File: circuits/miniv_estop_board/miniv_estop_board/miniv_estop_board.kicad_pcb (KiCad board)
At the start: 2 copper layers, 100 x 130 mm, 39 parts, among them J1 Conn_Main_DCDC, J2 Conn_neopixel_01, J3 Conn_neopixel_02, J4 Conn_neopixel_03, J5 Conn_neopixel_04, J6 EStop_button, J7 EStop_signal0, J8 EStop_signal1, Q1 2SJ555-E, Q2 NPN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

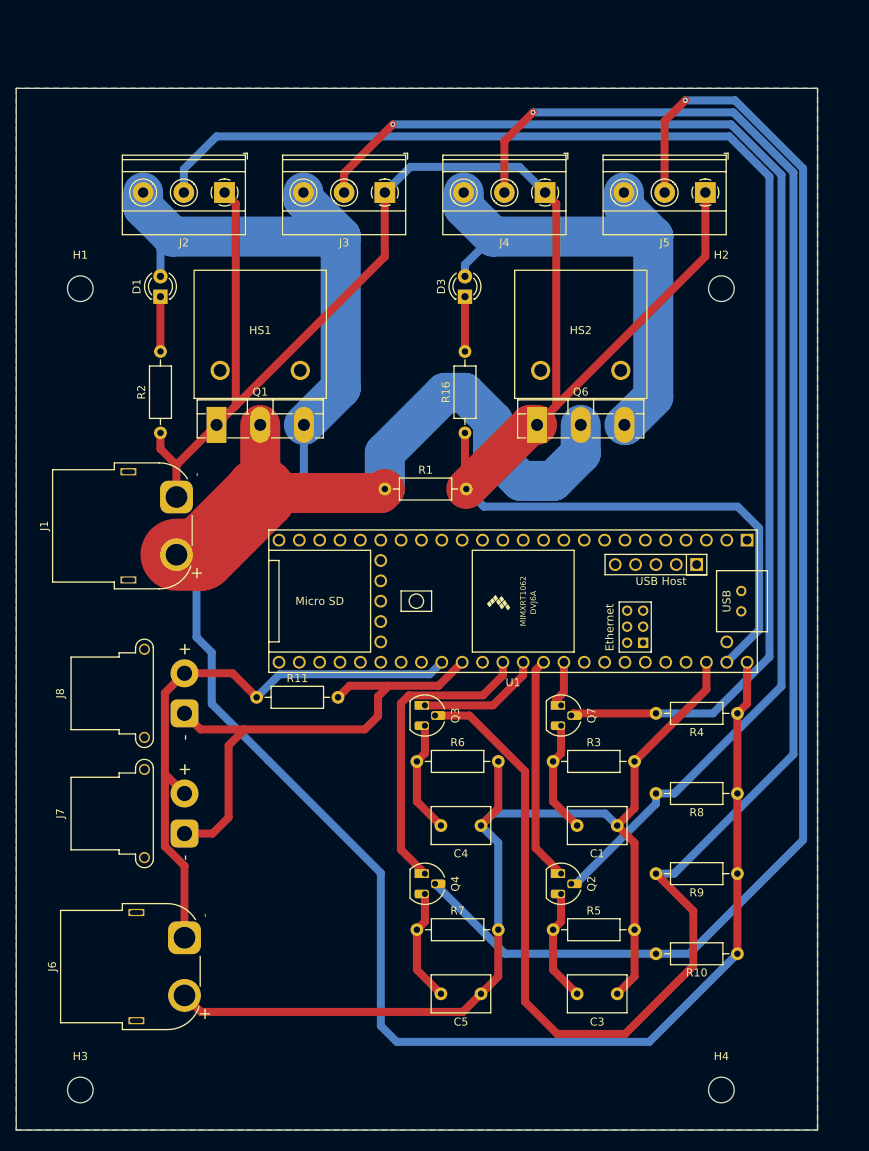
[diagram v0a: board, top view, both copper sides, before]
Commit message: modify connection
Signed-off-by: Masaya Kataoka <ms.kataoka@gmail.com>
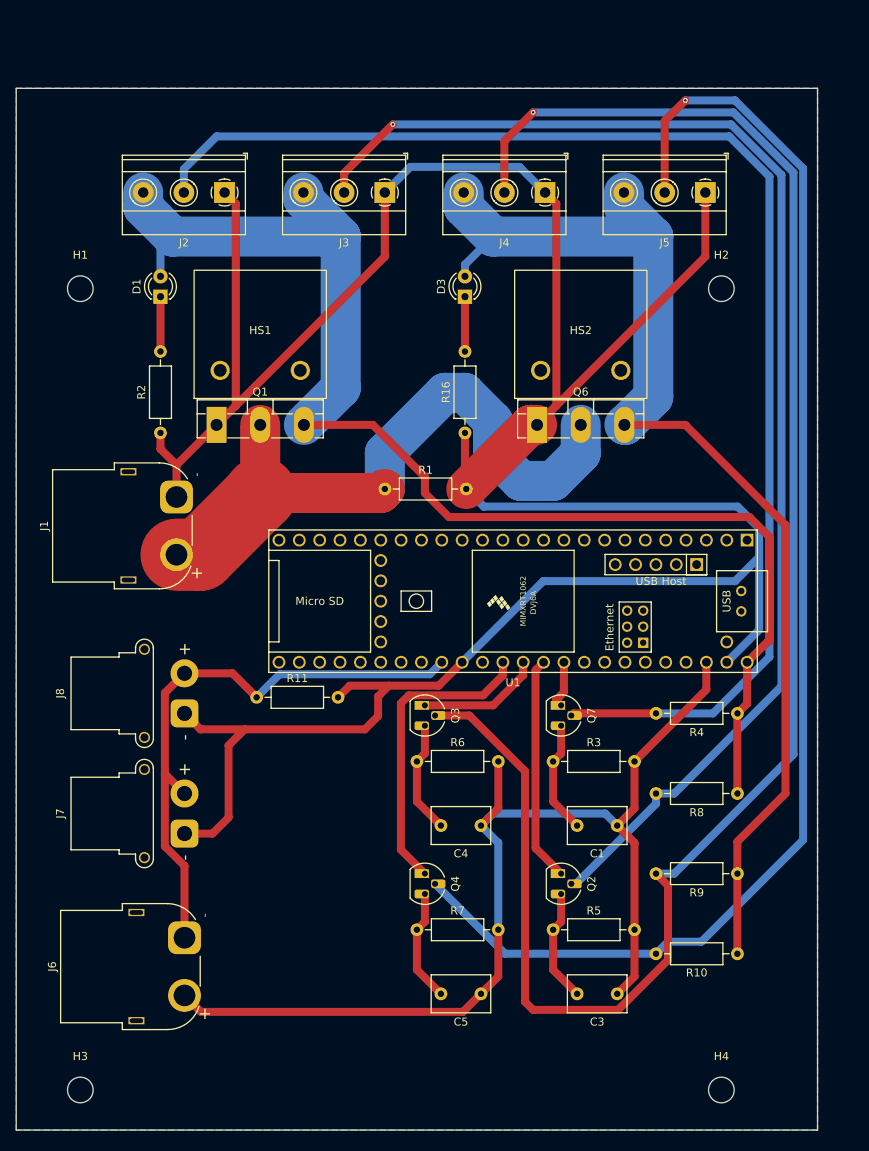
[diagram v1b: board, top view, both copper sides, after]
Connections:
- J1 pad 1: Net-(J1-Pin_1) -> GND
- J2 pad 1: Net-(J1-Pin_1) -> GND
- J3 pad 1: Net-(J1-Pin_1) -> GND
- J4 pad 1: Net-(J1-Pin_1) -> GND
- J5 pad 1: Net-(J1-Pin_1) -> GND
- Q1 pad 1: Net-(J1-Pin_1) -> GND
- Q6 pad 1: Net-(J1-Pin_1) -> GND
- R1 pad 2: Net-(J1-Pin_1) -> GND
- R10 pad 1: Net-(D1-A) -> Net-(D3-A)
- R16 pad 1: Net-(J1-Pin_1) -> GND
- R2 pad 1: Net-(J1-Pin_1) -> GND
- R9 pad 1: Net-(D1-A) -> Net-(D3-A)
- U1 pad 47: Net-(J1-Pin_1) -> GND
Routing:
- net GND: track 65.5 -> 355.9 mm
- net Net-(J1-Pin_1): track 247.9 -> 0.00 mm
- net Net-(D3-A): track 65.5 -> 146.8 mm
- net Net-(D1-A): track 243.3 -> 165.3 mm
- net Net-(J4-Pin_2): track 225.5 -> 218.2 mm

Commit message: add capaciter
Signed-off-by: Masaya Kataoka <ms.kataoka@gmail.com>
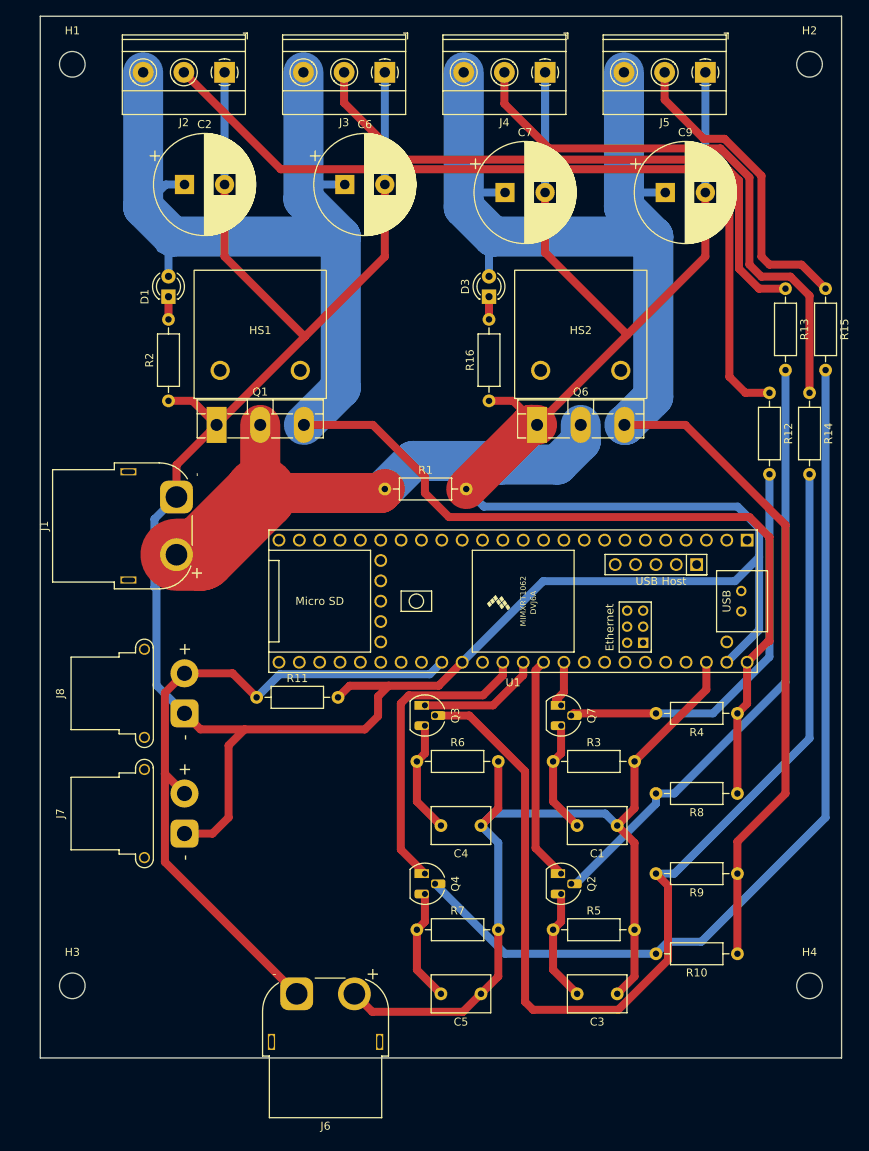
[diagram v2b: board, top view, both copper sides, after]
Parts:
- added C2: 1000μ, Capacitor_THT:CP_Radial_D12.5mm_P5.00mm, F.Cu at (110.0, 34.0)
- added C6: 1000μ, Capacitor_THT:CP_Radial_D12.5mm_P5.00mm, F.Cu at (130.0, 34.0)
- added C7: 1000μ, Capacitor_THT:CP_Radial_D12.5mm_P5.00mm, F.Cu at (150.0, 35.0)
- added C9: 1000μ, Capacitor_THT:CP_Radial_D12.5mm_P5.00mm, F.Cu at (170.0, 35.0)
- added R12: 470, Resistor_THT:R_Axial_DIN0207_L6.3mm_D2.5mm_P10.16mm_Horizontal, F.Cu at (183.0, 60.0)
- added R13: 470, Resistor_THT:R_Axial_DIN0207_L6.3mm_D2.5mm_P10.16mm_Horizontal, F.Cu at (185.0, 47.0)
- added R14: 470, Resistor_THT:R_Axial_DIN0207_L6.3mm_D2.5mm_P10.16mm_Horizontal, F.Cu at (188.0, 60.0)
- added R15: 470, Resistor_THT:R_Axial_DIN0207_L6.3mm_D2.5mm_P10.16mm_Horizontal, F.Cu at (190.0, 47.0)
- moved H2 30.1 mm to (188.0, 19.0)
- moved H1 28.0 mm to (96.0, 19.0)
- moved H4 17.0 mm to (188.0, 134.0)
- moved J6 15.7 mm to (124.0, 135.0), turned to 180 degrees
- moved J2 15.0 mm to (115.0, 20.0)
- moved J3 15.0 mm to (135.0, 20.0)
- moved J4 15.0 mm to (155.0, 20.0)
- moved J5 15.0 mm to (175.0, 20.0)
- moved H3 13.0 mm to (96.0, 134.0)
- moved R16 5.00 mm to (148.0, 61.0)
- moved R2 4.12 mm to (108.0, 61.0)
- moved D3 3.00 mm to (148.0, 48.0)
- moved D1 1.00 mm to (108.0, 48.0)
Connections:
- Q2 pad 2: Net-(J3-Pin_2) -> Net-(Q2-C)
- Q3 pad 2: Net-(J4-Pin_2) -> Net-(Q3-C)
- Q4 pad 2: Net-(J5-Pin_2) -> Net-(Q4-C)
- Q7 pad 2: Net-(J2-Pin_2) -> Net-(Q7-C)
- R10 pad 2: Net-(J5-Pin_2) -> Net-(Q4-C)
- R4 pad 2: Net-(J2-Pin_2) -> Net-(Q7-C)
- R8 pad 2: Net-(J3-Pin_2) -> Net-(Q2-C)
- R9 pad 2: Net-(J4-Pin_2) -> Net-(Q3-C)
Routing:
- net Net-(J4-Pin_2): track 218.2 -> 70.4 mm, vias 1 -> 0
- net Net-(Q3-C): track 0.00 -> 134.2 mm
- net Net-(J5-Pin_2): track 170.0 -> 39.2 mm, vias 1 -> 0
- net Net-(Q4-C): track 0.00 -> 115.2 mm
- net Net-(J3-Pin_2): track 163.1 -> 74.9 mm, vias 1 -> 0
- net Net-(Q2-C): track 0.00 -> 76.9 mm
- net Net-(J2-Pin_2): track 167.5 -> 103.7 mm
- net GND: track 355.9 -> 412.1 mm
- net Net-(Q7-C): track 0.00 -> 50.6 mm
- net Net-(D1-A): track 165.3 -> 209.2 mm
- net Net-(D3-A): track 146.8 -> 187.4 mm
- net Net-(J6-Pin_2): track 136.5 -> 115.4 mm
- net Net-(J1-Pin_2): track 81.9 -> 67.3 mm
- net Net-(J6-Pin_1): track 73.7 -> 86.5 mm
- net Net-(D3-K): track 6.84 -> 2.84 mm
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- removed copper zone on B.Cu, net GND
- removed copper zone on F.Cu, net GND

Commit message: update pcb
Signed-off-by: Masaya Kataoka <ms.kataoka@gmail.com>
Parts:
- moved H3 3.00 mm to (96.0, 137.0)
- moved H4 3.00 mm to (188.0, 137.0)
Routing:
- net Net-(D1-A): track 209.2 -> 207.1 mm
- added copper zone on B.Cu, net GND
- added copper zone on F.Cu, net GND
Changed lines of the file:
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@@
 			(layer "F.Fab")
 		)
-		(fp_text user "-"
-			(at 2.8 2.5 90)
+		(fp_text user "+"
+			(at -9.5 2.5 90)
 			(layer "F.SilkS")
 			(effects
 				(font
-					(size 1 1)
+					(size 1.5 1.5)
 					(thickness 0.15)
 				)
 			)
 		)
-		(fp_text user "+"
-			(at -9.5 2.5 90)
+		(fp_text user "-"
+			(at 2.8 2.5 90)
 			(layer "F.SilkS")
 			(effects
 				(font
-					(size 1.5 1.5)
+					(size 1 1)
 					(thickness 0.15)
 				)
@@
 		(tags "Resistor Axial_DIN0207 series Axial Horizontal pin pitch 10.16mm 0.25W = 1/4W length 6.3mm diameter 2.5mm")
 		(property "Reference" "R13"
-			(at 5.08 -2.37 -90)
+			(at 3.5 2.5 -90)
 			(layer "F.SilkS")
 			(effects
@@
 		)
 		(property "Value" "470"
-			(at 5.08 2.37 -90)
+			(at 7 2.5 -90)
 			(layer "F.Fab")
 			(effects
@@
 		(tags "Resistor Axial_DIN0207 series Axial Horizontal pin pitch 10.16mm 0.25W = 1/4W length 6.3mm diameter 2.5mm")
 		(property "Reference" "R12"
-			(at 5.08 -2.37 -90)
+			(at 3 2.5 -90)
 			(layer "F.SilkS")
 			(effects
@@
 		)
 		(property "Value" "470"
-			(at 5.08 2.37 -90)
+			(at 7 2.37 -90)
 			(layer "F.Fab")
 			(effects
@@
 		(tags "LED diameter 3.0mm 2 pins")
 		(property "Reference" "D1"
-			(at 0 -2.96 90)
+			(at 1.27 -2.96 90)
 			(layer "F.SilkS")
 			(effects
@@
 		)
 		(property "Value" "LED"
-			(at 3 -3 90)
+			(at 1.27 2.96 90)
 			(layer "F.Fab")
 			(effects
@@
 		(tags "Resistor Axial_DIN0207 series Axial Horizontal pin pitch 10.16mm 0.25W = 1/4W length 6.3mm diameter 2.5mm")
 		(property "Reference" "R15"
-			(at 5.08 -2.37 -90)
+			(at 3 2.5 -90)
 			(layer "F.SilkS")
 			(effects
@@
 		)
 		(property "Value" "470"
-			(at 5.08 2.37 -90)
+			(at 6.5 2.5 -90)
 			(layer "F.Fab")
 			(effects
@@
 	(footprint "MountingHole:MountingHole_3.2mm_M3"
 		(layer "F.Cu")
-		(at 188 134)
+		(at 188 137)
 		(descr "Mounting Hole 3.2mm, no annular, M3")
 		(tags "mounting hole 3.2mm no annular m3")
@@
 			(layer "F.Fab")
 		)
-		(fp_text user "-"
-			(at -3 0 90)
+		(fp_text user "+"
+			(at 8 0 90)
 			(layer "F.SilkS")
 			(effects
@@
 			)
 		)
-		(fp_text user "+"
-			(at 8 0 90)
+		(fp_text user "-"
+			(at -3 0 90)
 			(layer "F.SilkS")
 			(effects
@@
 	(footprint "MountingHole:MountingHole_3.2mm_M3"
 		(layer "F.Cu")
-		(at 96 134)
+		(at 96 137)
 		(descr "Mounting Hole 3.2mm, no annular, M3")
 		(tags "mounting hole 3.2mm no annular m3")
@@
 		(tags "Resistor Axial_DIN0207 series Axial Horizontal pin pitch 10.16mm 0.25W = 1/4W length 6.3mm diameter 2.5mm")
 		(property "Reference" "R14"
-			(at 5.08 -2.37 -90)
+			(at 3 2.5 -90)
 			(layer "F.SilkS")
 			(effects
@@
 		)
 		(property "Value" "470"
-			(at 5.08 2.37 -90)
+			(at 7 2.37 -90)
 			(layer "F.Fab")
 			(effects
@@
 		)
 		(property "Value" "MountingHole"
-			(at 0 4.2 0)
+			(at -3 4.5 0)
 			(layer "F.Fab")
 			(effects
@@
 		)
 		(property "Value" "MountingHole"
-			(at 2.5 4.5 0)
+			(at 4 6.5 90)
 			(layer "F.Fab")
 			(effects
@@
 			(layer "F.Fab")
 		)
-		(fp_text user "-"
-			(at 2.8 2.5 180)
+		(fp_text user "+"
+			(at -9.5 2.5 180)
 			(layer "F.SilkS")
 			(effects
 				(font
-					(size 1 1)
+					(size 1.5 1.5)
 					(thickness 0.15)
 				)
 			)
 		)
-		(fp_text user "+"
-			(at -9.5 2.5 180)
+		(fp_text user "-"
+			(at 2.8 2.5 180)
 			(layer "F.SilkS")
 			(effects
 				(font
-					(size 1.5 1.5)
+					(size 1 1)
 					(thickness 0.15)
 				)
@@
 	)
 	(segment
-		(start 107 42.001523)
-		(end 108.501523 40.5)
-		(width 1)
-		(layer "B.Cu")
-		(net 6)
-	)
-	(segment
 		(start 130 34)
 		(end 126.68 34)
@@
 	)
 	(segment
-		(start 153.16 64)
-		(end 145.16 72)
-		(width 5)
-		(layer "F.Cu")
-		(net 11)
-	)
-	(segment
 		(start 129.16 98)
 		(end 130.61 96.55)
@@
 	)
 	(segment
-		(start 109 73)
-		(end 109 69)
+		(start 175 43)
+		(end 175 35)
 		(width 1)
 		(layer "F.Cu")
@@
 	)
 	(segment
-		(start 175 43)
-		(end 175 35)
+		(start 148 69.16)
+		(end 145.16 72)
 		(width 1)
 		(layer "F.Cu")
@@
 	)
 	(segment
-		(start 109 69)
-		(end 114 64)
-		(width 1)
-		(layer "F.Cu")
-		(net 11)
-	)
-	(segment
 		(start 155 42.5)
 		(end 155 35)
@@
 	)
 	(segment
-		(start 154 64)
-		(end 153.16 64)
-		(width 5)
-		(layer "F.Cu")
-		(net 11)
-	)
-	(segment
 		(start 165.25 52.75)
 		(end 155 42.5)
@@
 	)
 	(segment
+		(start 148 61)
+		(end 148 69.16)
+		(width 1)
+		(layer "F.Cu")
+		(net 11)
+	)
+	(segment
 		(start 165.25 52.75)
 		(end 154 64)
@@
 	)
 	(segment
+		(start 114 64)
+		(end 114 68)
+		(width 1)
+		(layer "B.Cu")
+		(net 11)
+	)
+	(segment
 		(start 181.71 80.5)
 		(end 181.71 89.58)
@@
 	)
 	(segment
+		(start 114 68)
+		(end 109 73)
+		(width 1)
+		(layer "B.Cu")
+		(net 11)
+	)
+	(segment
 		(start 106.25 75.75)
 		(end 106.25 84.25)
@@
 		(net 82)
 	)
+	(zone
+		(net 11)
+		(net_name "GND")
+		(layers "F&B.Cu")
+		(hatch edge 0.5)
+		(connect_pads
+			(clearance 0.5)
+		)
+		(min_thickness 0.25)
+		(filled_areas_thickness no)
+		(fill yes
+			(thermal_gap 0.5)
+			(thermal_bridge_width 0.5)
+		)
+		(polygon
+			(pts
+				(xy 192 13) (xy 92 13) (xy 92 143) (xy 192 143)
+			)
+		)
+	)
 )
